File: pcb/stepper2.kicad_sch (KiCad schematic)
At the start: 49 parts, among them J1 DA15_Receptacle_MountingHoles, J10 Conn_01x07_Pin, J2 DA15_Receptacle_MountingHoles, J3 DA15_Receptacle_MountingHoles, J4 DE15_Receptacle_HighDensity, J5 DE15_Receptacle_HighDensity, J6 DE15_Receptacle_HighDensity, J7 Conn_01x04_Pin, J8 Conn_01x05_Pin, J9 Conn_01x06_Pin, SW1 SW_Push, U1 AM26LS32ACN, U2 AM26LS32Ax, U3 AM26LS32ACN, U4 TMC2209_BIGTREETECH, U5 TMC2209_BIGTREETECH, U6 TMC2209_BIGTREETECH

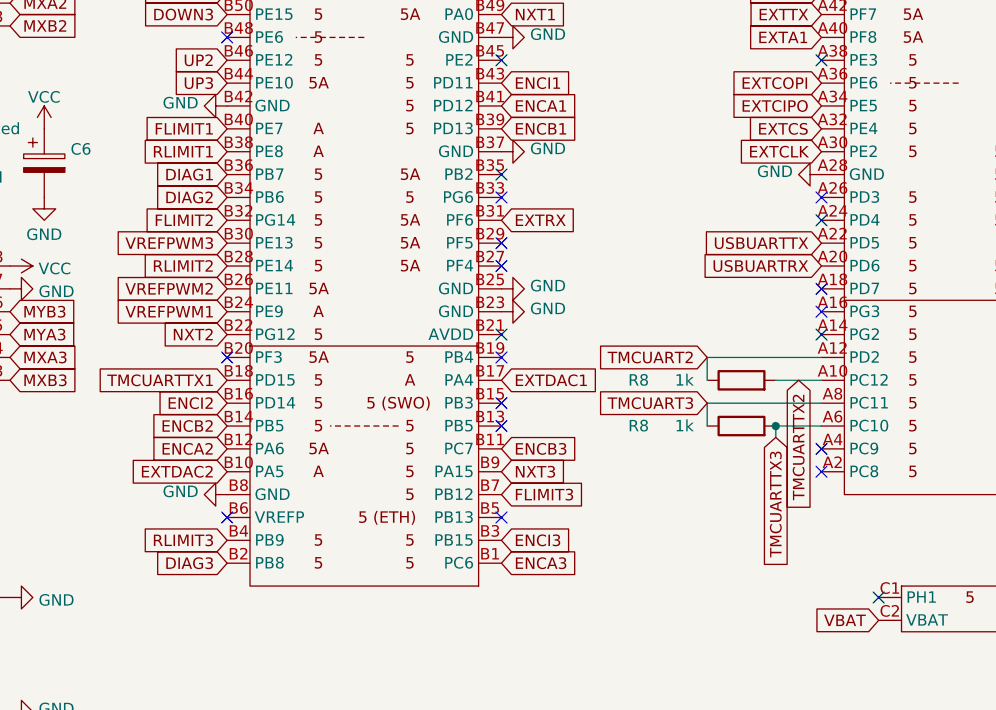
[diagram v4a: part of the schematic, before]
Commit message: DIR and EN pins connected to GPIO
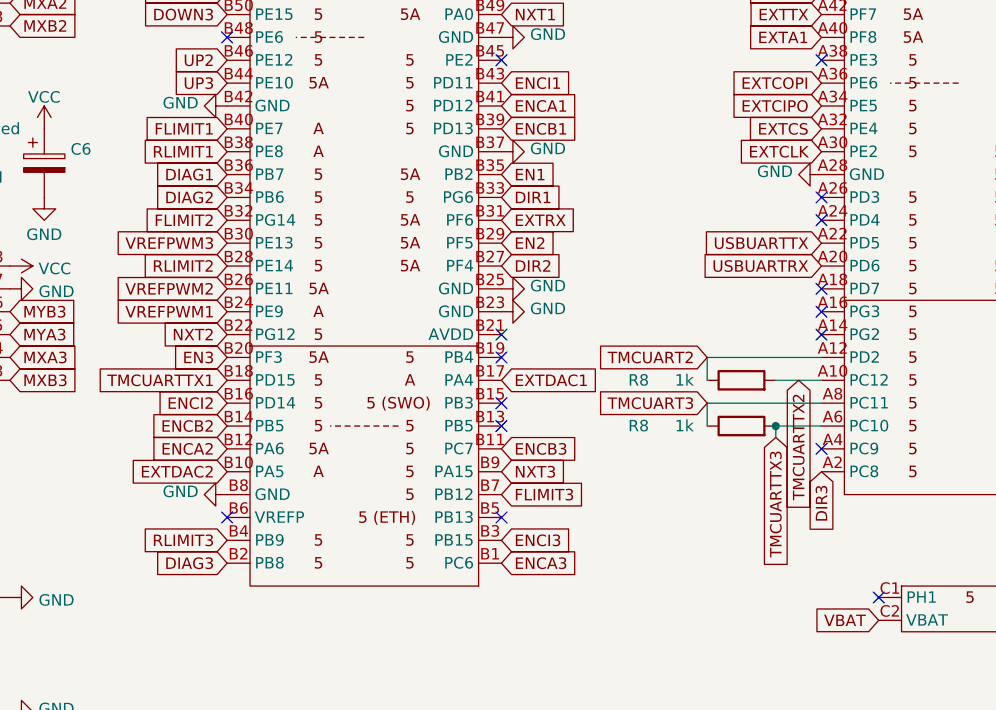
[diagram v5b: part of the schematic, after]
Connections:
- net DIR1: now also U10.B33 (PG6)
- net DIR2: now also U10.B27 (PF4)
- net DIR3: now also U10.A2 (PC8)
- net EN1: now also U10.B35 (PB2)
- net EN2: now also U10.B29 (PF5)
- net EN3: now also U10.B20 (PF3)
- no-connect marks 97 -> 91
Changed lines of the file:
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@@
   (no_connect (at 21.59 160.02))
   (no_connect (at 271.78 106.68))
-  (no_connect (at 205.74 111.76))
-  (no_connect (at 175.26 129.54))
   (no_connect (at 251.46 19.05))
-  (no_connect (at 205.74 109.22))
+  (no_connect (at 205.74 96.52))
   (no_connect (at 21.59 100.33))
   (no_connect (at 21.59 33.02))
@@
   (no_connect (at 270.51 33.02))
   (no_connect (at 128.27 95.25))
-  (no_connect (at 205.74 116.84))
   (no_connect (at 205.74 129.54))
   (no_connect (at 21.59 147.32))
@@
   (no_connect (at 113.03 55.88))
   (no_connect (at 113.03 116.84))
-  (no_connect (at 241.3 142.24))
-  (no_connect (at 205.74 96.52))
   (no_connect (at 242.57 33.02))
   (no_connect (at 205.74 147.32))
@@
   (no_connect (at 97.79 129.54))
   (no_connect (at 241.3 139.7))
-  (no_connect (at 205.74 119.38))
   (no_connect (at 205.74 134.62))
   (no_connect (at 241.3 111.76))
@@
     )
   )
+  (global_label "DIR2" (shape input) (at 205.74 119.38 0) (fields_autoplaced)
+    (effects (font (size 1.27 1.27)) (justify left))
+    (property "Intersheetrefs" "${INTERSHEET_REFS}" (at 213.0001 119.38 0)
+      (effects (font (size 1.27 1.27)) (justify left) hide)
+    )
+  )
   (global_label "ENCA1" (shape input) (at 205.74 101.6 0) (fields_autoplaced)
     (effects (font (size 1.27 1.27)) (justify left))
@@
     )
   )
+  (global_label "EN1" (shape input) (at 205.74 109.22 0) (fields_autoplaced)
+    (effects (font (size 1.27 1.27)) (justify left))
+    (property "Intersheetrefs" "${INTERSHEET_REFS}" (at 212.3348 109.22 0)
+      (effects (font (size 1.27 1.27)) (justify left) hide)
+    )
+  )
   (global_label "ENCB3+" (shape input) (at 50.8 152.4 180) (fields_autoplaced)
     (effects (font (size 1.27 1.27)) (justify right))
     (property "Intersheetrefs" "${INTERSHEET_REFS}" (at 40.0928 152.4 0)
       (effects (font (size 1.27 1.27)) (justify right) hide)
+    )
+  )
+  (global_label "DIR1" (shape input) (at 205.74 111.76 0) (fields_autoplaced)
+    (effects (font (size 1.27 1.27)) (justify left))
+    (property "Intersheetrefs" "${INTERSHEET_REFS}" (at 213.0001 111.76 0)
+      (effects (font (size 1.27 1.27)) (justify left) hide)
     )
   )
@@
     )
   )
+  (global_label "EN3" (shape input) (at 175.26 129.54 180) (fields_autoplaced)
+    (effects (font (size 1.27 1.27)) (justify right))
+    (property "Intersheetrefs" "${INTERSHEET_REFS}" (at 168.6652 129.54 0)
+      (effects (font (size 1.27 1.27)) (justify right) hide)
+    )
+  )
   (global_label "MYA1" (shape input) (at 99.06 21.59 270) (fields_autoplaced)
     (effects (font (size 1.27 1.27)) (justify right))
@@
     )
   )
+  (global_label "EN2" (shape input) (at 205.74 116.84 0) (fields_autoplaced)
+    (effects (font (size 1.27 1.27)) (justify left))
+    (property "Intersheetrefs" "${INTERSHEET_REFS}" (at 212.3348 116.84 0)
+      (effects (font (size 1.27 1.27)) (justify left) hide)
+    )
+  )
   (global_label "EXTCS" (shape input) (at 241.3 104.14 180) (fields_autoplaced)
     (effects (font (size 1.27 1.27)) (justify right))
@@
       (effects (font (size 1.27 1.27)) (justify right) hide)
     )
+  )
+  (global_label "DIR3" (shape input) (at 241.3 142.24 270) (fields_autoplaced)
+    (effects (font (size 1.27 1.27)) (justify right))
+    (property "Intersheetrefs" "${INTERSHEET_REFS}" (at 241.3 149.5001 90)
+      (effects (font (size 1.27 1.27)) (justify right) hide)
+    )

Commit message: First complete version of the PCB
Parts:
- added H1, H2: MountingHole, stepper2:MountingHole_3.2mm_M3, symbol Mechanical:MountingHole
- added J11: FAN, Connector_JST:JST_XH_B2B-XH-AM_1x02_P2.50mm_Vertical, symbol Connector:Conn_01x02_Pin
- C19: value 2u2 -> 22u
- C4, C5, C6: value C_Polarized -> 24V
- C7: value C_Polarized -> 5V
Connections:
- net +5V: now also J11.2 (Pin_2)
- net GND: now also J11.1 (Pin_1)
- no-connect marks 91 -> 94

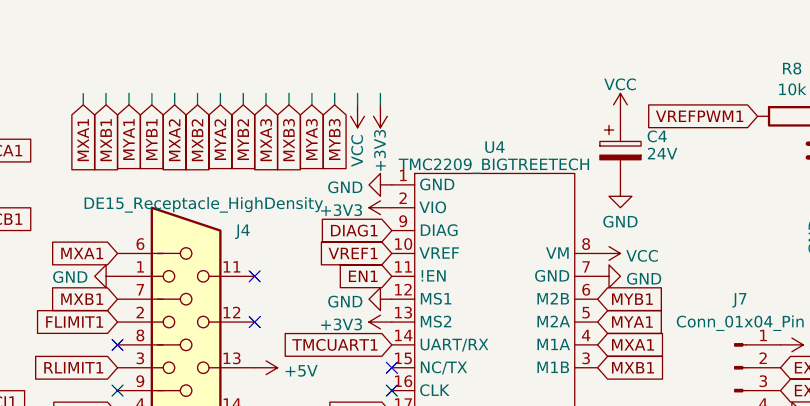
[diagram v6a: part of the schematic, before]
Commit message: Revert to 2 layer PCB
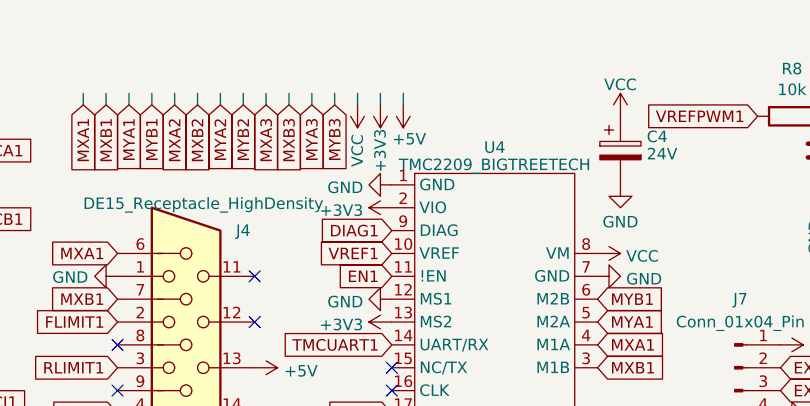
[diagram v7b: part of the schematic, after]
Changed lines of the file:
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@@
     (stroke (width 0) (type default))
   )
+  (wire (pts (xy 129.54 20.32) (xy 129.54 21.59))
+    (stroke (width 0) (type default))
+  )
   (wire (pts (xy 236.22 137.16) (xy 241.3 137.16))
     (stroke (width 0) (type default))
@@
     )
   )
+  (netclass_flag "" (length 2.54) (shape round) (at 129.54 20.32 0)
+    (effects (font (size 1.27 1.27)) (justify left bottom))
+    (property "Netclass" "thick" (at 129.54 16.51 90)
+      (effects (font (size 1.27 1.27) italic) (justify left))
+    )
+  )
   (netclass_flag "" (length 2.54) (shape round) (at 93.98 20.32 0)
     (effects (font (size 1.27 1.27)) (justify left bottom))
@@
         )
       )
+    )
+  )
+  (symbol (lib_id "power:+5V") (at 129.54 21.59 180) (unit 1)
+    (in_bom yes) (on_board yes) (dnp no)
+    (property "Reference" "#PWR0103" (at 129.54 17.78 0)
+      (effects (font (size 1.27 1.27)) hide)
+    )
+    (property "Value" "+5V" (at 132.08 25.4 0)
+      (effects (font (size 1.27 1.27)) (justify left))
+    )
+    (property "Footprint" "" (at 129.54 21.59 0)
+      (effects (font (size 1.27 1.27)) hide)
+    )
+    (property "Datasheet" "" (at 129.54 21.59 0)
+      (effects (font (size 1.27 1.27)) hide)
+    )
+    (pin "1")
+    (instances
+      (project "stepper2"
+        (path "/2519ce93-57a7-4269-80ad-e58f985d69b8"
+          (reference "#PWR0103") (unit 1)
+        )
+      )
+      (project "stepper"
+        (path "/29e6b2c4-71e3-4cf4-b657-cab9f28c2e75"
+          (reference "#PWR0117") (unit 1)
+        )
+      )
